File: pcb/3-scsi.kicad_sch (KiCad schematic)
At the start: 0 parts

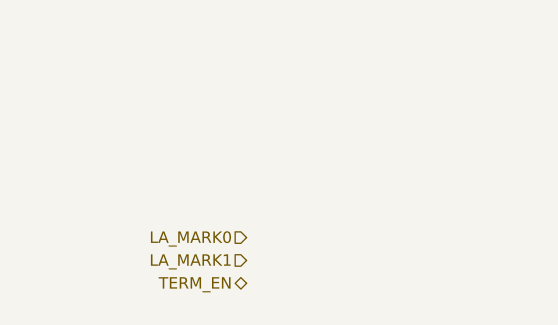
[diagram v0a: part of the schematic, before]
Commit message: Phase 3: populate power sheet; descriptive net names
Power sheet: bench eFuse (TPS259470A) with UVLO/OVLO string and EN
clamp, TPS2116 bench-priority mux with VBUS snubber, 3.3 V and 2.83 V
TPS73701 LDOs. Notes on the string's tap voltages, eFuse setting pins
and every DNP part. Project symbol library with the TPS259470A and
TPS73701DCQ drawn from the datasheet pin tables.

Nets renamed to spelled-out names (IS_BENCH_POWERED, *_INVERTED for
active-low, FEEDBACK, VTERMINATOR, TERMINATOR_EN) across the schematic,
pinout page, parts list and power block page.

Co-Authored-By: Claude Opus 5.5 <noreply@anthropic.com>
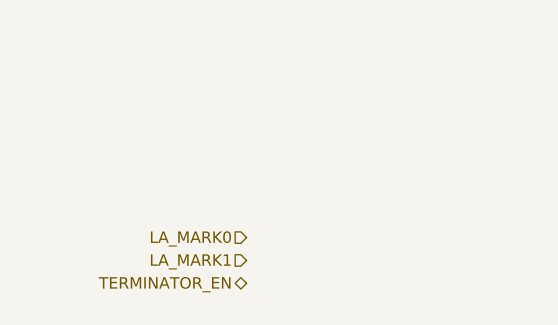
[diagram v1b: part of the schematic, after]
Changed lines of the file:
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@@
 	(hierarchical_label "LA_MARK0" (shape input) (at 50.8 243.84 180) (effects (font (size 1.27 1.27)) (justify right)))
 	(hierarchical_label "LA_MARK1" (shape input) (at 50.8 246.38 180) (effects (font (size 1.27 1.27)) (justify right)))
-	(hierarchical_label "TERM_EN" (shape bidirectional) (at 50.8 248.92 180) (effects (font (size 1.27 1.27)) (justify right)))
+	(hierarchical_label "TERMINATOR_EN" (shape bidirectional) (at 50.8 248.92 180) (effects (font (size 1.27 1.27)) (justify right)))
 	(embedded_fonts no)
 )
